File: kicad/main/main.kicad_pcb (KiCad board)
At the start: 2 copper layers, 31.9 x 22.7 mm, 54 parts, among them J1 Conn_01x02, J2 Conn_01x03, J3 Conn_01x03, J4 Conn_01x02, J5 Conn_01x02, J6 Connector, USB-TYPE-C-16P, J7 Conn_01x02, J8 Conn_01x02, J9 Conn_01x03, U1 CL6807, U2 XC6206P332MR, U5 RP2040, X1 X322512MSB4SI

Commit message: Prorgess on PCB
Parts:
- removed D1: SS14, PCM_JLCPCB:D_SMA
- removed J9: Conn_01x03, Connector_PinHeader_2.54mm:PinHeader_1x03_P2.54mm_Vertical
- removed L1: 68uH, EasyEDA_Lib:IND-SMD_L6.0-W6.0_FNR60XXS
- removed R1: 150mΩ, Resistor_SMD:R_1206_3216Metric_Pad1.30x1.75mm_HandSolder
- removed U1: CL6807, EasyEDA_Lib:SOT-89-5_L4.5-W2.5-P1.50-LS4.5-BR
- added J10: Conn_01x02, solder-pads:2-position, F.Cu at (124.3, 45.5)
- added JP1: SolderJumper_2_Open, Jumper:SolderJumper-2_P1.3mm_Open_Pad1.0x1.5mm, F.Cu at (125.4, 36.3)
- moved U2 60.0 mm to (129.1, 43.5)
- moved C15 58.9 mm to (119.8, 47.6), turned to 180 degrees
- moved J1 58.8 mm to (129.1, 32.5), turned to 90 degrees
- moved C16 55.4 mm to (120.0, 43.2), turned to 180 degrees
- moved J3 53.6 mm to (122.7, 32.5), turned to 90 degrees
- moved C10 53.3 mm to (115.2, 57.5)
- moved C11 53.3 mm to (115.2, 59.4)
- moved C12 53.3 mm to (115.2, 61.2)
- moved C13 53.3 mm to (115.2, 63.0)
- moved C14 53.3 mm to (115.2, 64.9)
- moved C3 53.3 mm to (112.3, 57.5)
- moved C4 53.3 mm to (112.3, 59.4)
- moved C5 53.3 mm to (112.3, 61.2)
- moved C6 53.3 mm to (112.3, 63.0)
- moved C7 53.3 mm to (112.3, 64.9)
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
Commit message: Progress on PCB
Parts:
- moved C9 33.6 mm to (117.9, 35.6), turned to 180 degrees
- moved C2 31.2 mm to (125.3, 41.3), turned to 180 degrees
- moved C1 29.8 mm to (129.1, 46.3)
- moved R6 27.2 mm to (107.1, 38.2)
- moved C6 25.7 mm to (113.3, 37.4)
- moved C13 21.2 mm to (120.0, 42.4)
- moved R2 18.1 mm to (107.7, 44.5), turned to 90 degrees
- moved C12 17.3 mm to (109.0, 45.0), turned to 180 degrees
- moved C5 17.3 mm to (109.0, 44.2), turned to 180 degrees
- moved R3 15.6 mm to (107.7, 49.5), turned to 90 degrees
- moved C11 12.0 mm to (109.6, 48.7), turned to -90 degrees
- moved C3 11.2 mm to (119.8, 49.2)
- moved C10 10.2 mm to (119.8, 48.4)
- moved C4 9.27 mm to (109.6, 50.5), turned to 90 degrees
- moved R10 5.00 mm to (121.9, 35.8), turned to 180 degrees
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
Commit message: Progress on PCB
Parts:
- removed C13: 1uF, PCM_JLCPCB:C_0402
- removed C14, C7, C8: 100nF, PCM_JLCPCB:C_0402
- TP2, TP3: moved to B.Cu
- moved TP4 32.2 mm to (119.9, 51.8)
- moved TP3 27.3 mm to (114.9, 55.4), turned to 180 degrees
- moved TP2 25.7 mm to (110.5, 55.5), turned to 180 degrees
- moved TP1 23.6 mm to (108.4, 51.6)
- moved TP6 22.4 mm to (108.2, 40.4)
- moved TP5 19.5 mm to (108.2, 42.6)
- moved C15 1.70 mm to (121.5, 47.3), turned to 0 degrees
- moved C4 1.30 mm to (110.3, 51.6), turned to -90 degrees
- moved C9 1.20 mm to (117.9, 36.8)
- moved C1 1.09 mm to (130.2, 46.1)
- moved R10 1.05 mm to (121.9, 36.9)
- moved R9 1.03 mm to (125.4, 39.3)
- moved R4 0.78 mm to (109.4, 47.2)
- moved R5 0.78 mm to (109.4, 46.0)
- moved C3 0.78 mm to (119.4, 48.5), turned to -90 degrees
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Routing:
- net +5V: track 0.00 -> 45.9 mm
- net +3.3V: track 0.00 -> 36.9 mm, vias 0 -> 6
- net QSPI_SD1: track 0.00 -> 26.1 mm, vias 0 -> 2
- net QSPI_SS: track 0.00 -> 25.4 mm, vias 0 -> 2
- net QSPI_SD2: track 0.00 -> 24.4 mm, vias 0 -> 2
- net Data In: track 0.00 -> 23.4 mm, vias 0 -> 2
- net Onboard LED: track 0.00 -> 22.4 mm, vias 0 -> 2
- net QSPI_SD0: track 0.00 -> 14.9 mm, vias 0 -> 2
- net QSPI_SCLK: track 0.00 -> 13.2 mm, vias 0 -> 2
- net LED-: track 0.00 -> 12.0 mm, vias 0 -> 1
- net +1.1V: track 0.00 -> 11.8 mm, vias 0 -> 2
- net QSPI_SD3: track 0.00 -> 10.8 mm, vias 0 -> 2
- net Net-(U5-XOUT): track 0.00 -> 7.97 mm, vias 0 -> 2
- net Net-(U5-XIN): track 0.00 -> 7.39 mm, vias 0 -> 2
- net Net-(U5-GPIO6): track 0.00 -> 5.60 mm
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
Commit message: Progress on PCB design
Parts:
- added C13: 1uF, PCM_JLCPCB:C_0402, F.Cu at (109.8, 51.8)
- added H1: MountingHole, MountingHole:MountingHole_2.5mm, F.Cu at (129.9, 54.6)
- added H2: MountingHole, MountingHole:MountingHole_2.5mm, F.Cu at (102.0, 54.6)
- added R1: 10kΩ, PCM_JLCPCB:R_0402, F.Cu at (115.1, 37.4)
- added R11: 10kΩ, PCM_JLCPCB:R_0402, F.Cu at (110.0, 31.9)
- TP2, TP3: moved to F.Cu
- moved TP2 4.65 mm to (114.6, 53.2), turned to 0 degrees
- moved TP1 3.12 mm to (111.2, 53.0)
- moved TP3 2.56 mm to (116.5, 53.4), turned to 0 degrees
- moved TP4 1.86 mm to (118.5, 53.0)
- moved J7 0.88 mm to (123.8, 50.0)
- moved TP6 0.86 mm to (107.3, 40.5)
- moved C4 0.77 mm to (109.8, 51.0), turned to 180 degrees
- moved J8 0.62 mm to (128.8, 50.0)
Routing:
- net +5V: track 45.9 -> 85.0 mm, vias 0 -> 3
- net Tilt: track 0.00 -> 38.3 mm, vias 0 -> 3
- net Pan: track 0.00 -> 28.2 mm, vias 0 -> 2
- net +3.3V: track 36.9 -> 58.9 mm, vias 6 -> 8
- net +1.1V: track 11.8 -> 32.6 mm, vias 2 -> 4
- net Reset Button: track 0.00 -> 20.1 mm, vias 0 -> 2
- net T LED: track 0.00 -> 18.4 mm, vias 0 -> 1
- net QSPI_SS: track 25.4 -> 40.3 mm, vias 2 -> 6
- net T Board: track 0.00 -> 13.5 mm, vias 0 -> 1
- net Net-(U5-GPIO29_ADC3): track 0.00 -> 8.32 mm, vias 0 -> 2
- net Net-(U5-GPIO28_ADC2): track 0.00 -> 6.75 mm, vias 0 -> 2
- net Net-(U5-GPIO5): track 0.00 -> 3.22 mm
- net Net-(U5-GPIO0): track 5.04 -> 2.46 mm, vias 2 -> 0
- net Boot Button: track 0.00 -> 2.15 mm
- net Net-(U5-GPIO4): track 0.00 -> 2.08 mm
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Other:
- board size 31.9 x 22.7 mm -> 31.9 x 26.5 mm

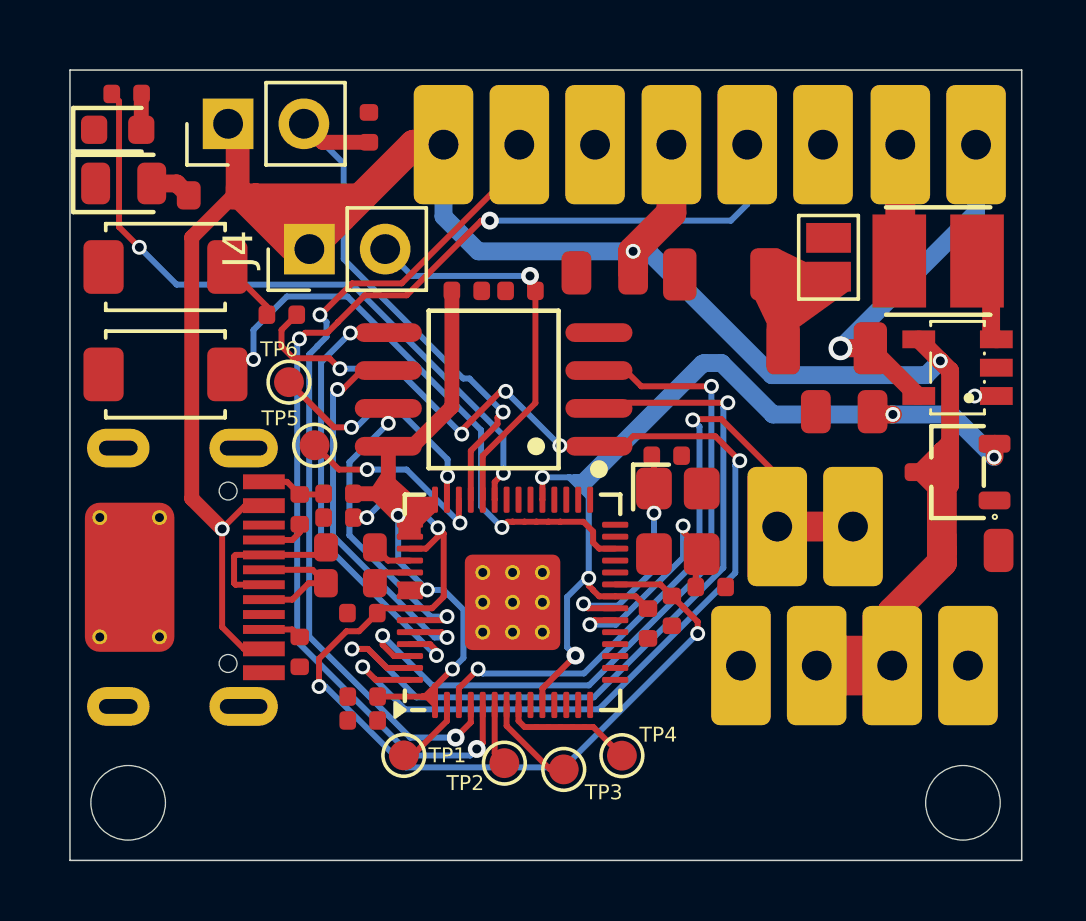
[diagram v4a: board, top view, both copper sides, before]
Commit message: PCB Progress and Added LED_PWM signal
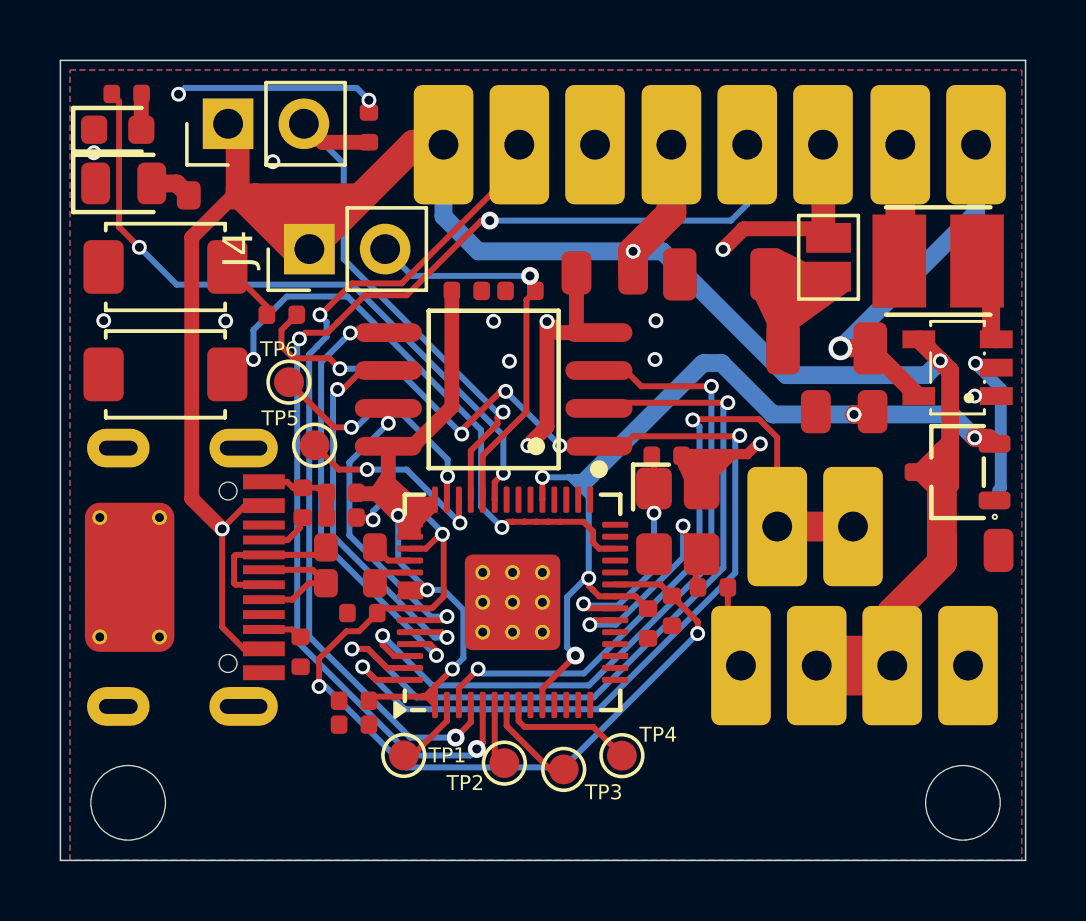
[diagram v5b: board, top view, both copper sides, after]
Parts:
- moved C13 0.32 mm to (109.5, 51.9)
- moved C4 0.32 mm to (109.5, 51.1)
- moved R2 0.25 mm to (107.8, 44.5)
- moved C5 0.10 mm to (109.1, 44.2)
- moved C12 0.10 mm to (109.1, 45.0)
- moved C15 0.08 mm to (121.5, 47.3)
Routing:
- net GND: track 2.19 -> 41.8 mm, vias 0 -> 15
- net Data In: track 23.2 -> 23.9 mm
- net QSPI_SS: track 40.3 -> 40.8 mm
- added copper zone on B.Cu, net GND
- added copper zone on F.Cu, net GND
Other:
- board size 31.9 x 26.5 mm -> 32.4 x 26.8 mm

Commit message: PCB Progress
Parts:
- moved C2 0.24 mm to (125.7, 41.5)
- moved U4 0.24 mm to (129.5, 40.0)
- moved R9 0.24 mm to (125.1, 39.3)
- moved C1 0.18 mm to (130.0, 46.1)
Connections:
- U5 pad 9: unconnected-(U5-GPIO7-Pad9) -> LED_PWM
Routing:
- net LED_PWM: track 0.73 -> 26.7 mm, vias 1 -> 2
- net GND: track 41.8 -> 63.6 mm, vias 15 -> 18
- net +3.3V: track 58.6 -> 67.2 mm
- net +5V: track 85.0 -> 86.4 mm, vias 3 -> 2
- net Net-(U5-XOUT): track 8.23 -> 7.04 mm

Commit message: PCB is just about finished
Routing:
- net GND: vias 18 -> 86

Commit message: Improved PCB design
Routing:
- net GND: track 63.6 -> 69.1 mm, vias 86 -> 44
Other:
- board text added: "+5V"
- board text added: "5V"
- board text added: "G"
- board text added: "GND"
- board text added: "Pan"
- board text added: "Tilt"
